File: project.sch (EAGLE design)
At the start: 43 parts, among them U1 DSPIC33FJ64MC804-H/PT, U2 TB6612FNG,C,8,EL, Y1 ABM8-20.000MHZ-B2-T

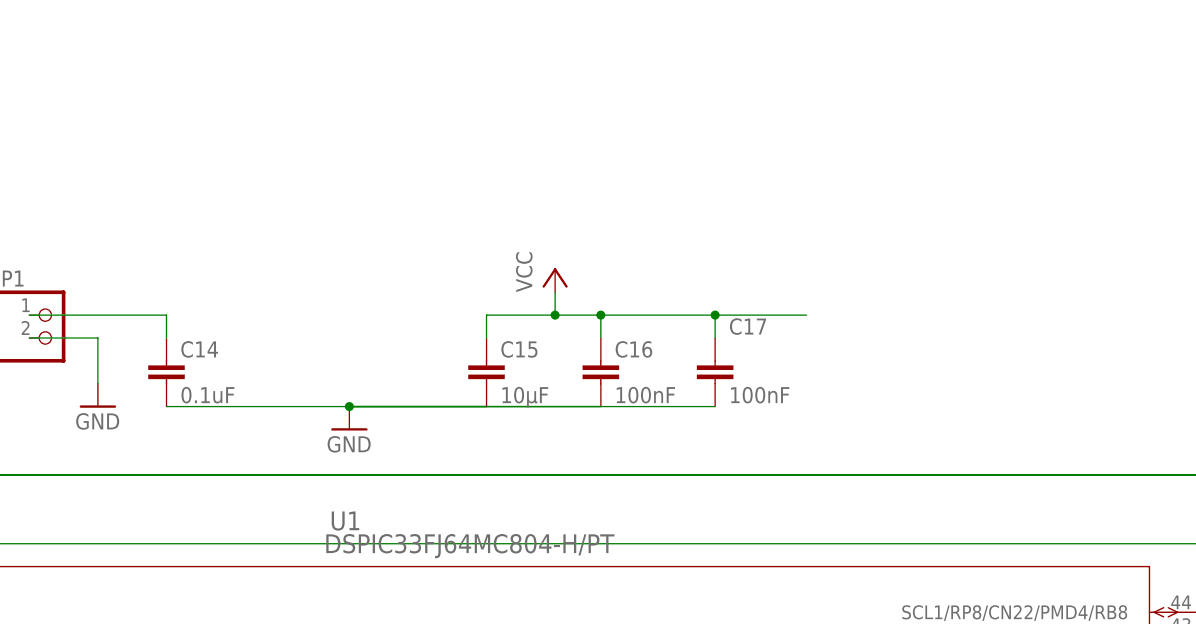
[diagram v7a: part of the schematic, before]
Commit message: Linear Regulator Added
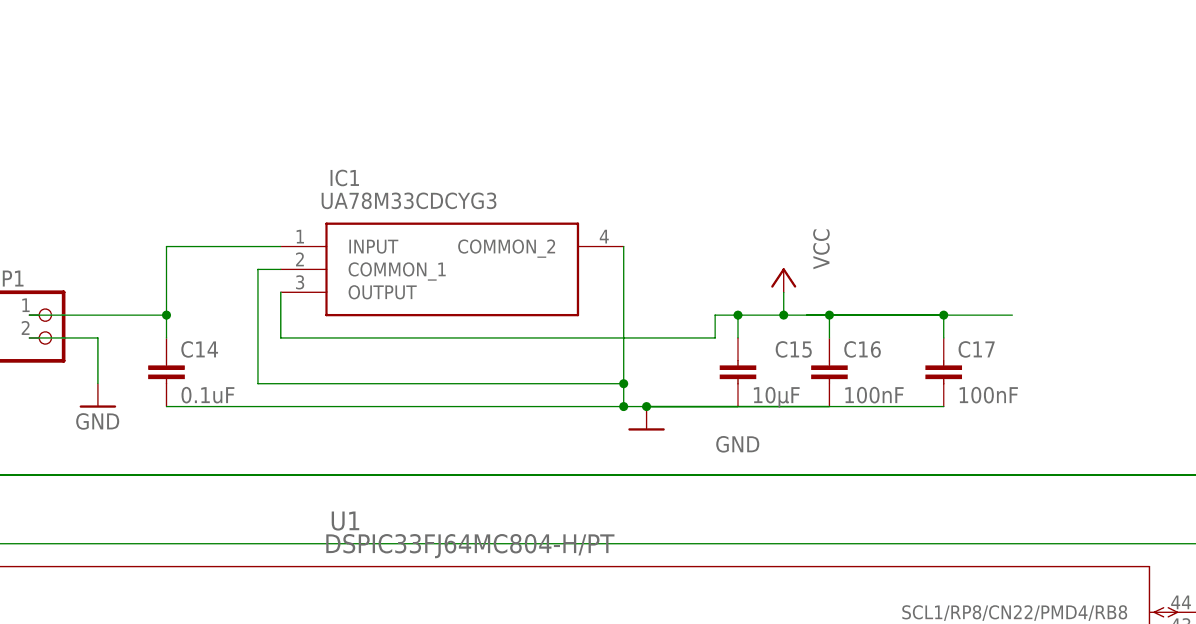
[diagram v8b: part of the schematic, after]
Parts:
- added IC1: UA78M33CDCYG3, UA78M33CDCYG3:UA78M33CDCYG3
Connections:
- net GND: now also IC1.COMMON_1, IC1.COMMON_2
- net N$6: now also IC1.INPUT
- net VCC: now also IC1.OUTPUT
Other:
- moved on the sheet: C15, C16, C17
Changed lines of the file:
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@@
 <part name="GND14" library="supply1" library_urn="urn:adsk.eagle:library:371" deviceset="GND" device=""/>
 <part name="GND15" library="supply1" library_urn="urn:adsk.eagle:library:371" deviceset="GND" device=""/>
+<part name="IC1" library="UA78M33CDCYG3" deviceset="UA78M33CDCYG3" device=""/>
 </parts>
 <sheets>
@@
 <attribute name="VALUE" x="9.144" y="48.641" size="1.778" layer="96"/>
 </instance>
-<instance part="C15" gate="G$1" x="43.18" y="53.34" smashed="yes">
-<attribute name="NAME" x="44.704" y="53.721" size="1.778" layer="95"/>
-<attribute name="VALUE" x="44.704" y="48.641" size="1.778" layer="96"/>
-</instance>
-<instance part="C16" gate="G$1" x="55.88" y="53.34" smashed="yes">
-<attribute name="NAME" x="57.404" y="53.721" size="1.778" layer="95"/>
-<attribute name="VALUE" x="57.404" y="48.641" size="1.778" layer="96"/>
-</instance>
-<instance part="C17" gate="G$1" x="68.58" y="53.34" smashed="yes">
-<attribute name="NAME" x="70.104" y="56.261" size="1.778" layer="95"/>
-<attribute name="VALUE" x="70.104" y="48.641" size="1.778" layer="96"/>
-</instance>
-<instance part="P+5" gate="VCC" x="50.8" y="63.5" smashed="yes">
-<attribute name="VALUE" x="48.26" y="60.96" size="1.778" layer="96" rot="R90"/>
-</instance>
-<instance part="GND19" gate="1" x="27.94" y="45.72" smashed="yes">
-<attribute name="VALUE" x="25.4" y="43.18" size="1.778" layer="96"/>
+<instance part="C15" gate="G$1" x="71.12" y="53.34" smashed="yes">
+<attribute name="NAME" x="75.184" y="53.721" size="1.778" layer="95"/>
+<attribute name="VALUE" x="72.644" y="48.641" size="1.778" layer="96"/>
+</instance>
+<instance part="C16" gate="G$1" x="81.28" y="53.34" smashed="yes">
+<attribute name="NAME" x="82.804" y="53.721" size="1.778" layer="95"/>
+<attribute name="VALUE" x="82.804" y="48.641" size="1.778" layer="96"/>
+</instance>
+<instance part="C17" gate="G$1" x="93.98" y="53.34" smashed="yes">
+<attribute name="NAME" x="95.504" y="53.721" size="1.778" layer="95"/>
+<attribute name="VALUE" x="95.504" y="48.641" size="1.778" layer="96"/>
+</instance>
+<instance part="P+5" gate="VCC" x="76.2" y="63.5" smashed="yes">
+<attribute name="VALUE" x="81.28" y="63.5" size="1.778" layer="96" rot="R90"/>
+</instance>
+<instance part="GND19" gate="1" x="60.96" y="45.72" smashed="yes">
+<attribute name="VALUE" x="68.58" y="43.18" size="1.778" layer="96"/>
 </instance>
 <instance part="GND20" gate="1" x="0" y="48.26" smashed="yes">
@@
 <instance part="GND15" gate="1" x="251.46" y="33.02" smashed="yes">
 <attribute name="VALUE" x="248.92" y="30.48" size="1.778" layer="96"/>
+</instance>
+<instance part="IC1" gate="G$1" x="20.32" y="66.04" smashed="yes">
+<attribute name="NAME" x="29.21" y="73.66" size="1.778" layer="95" rot="R180" align="center-left"/>
+<attribute name="VALUE" x="44.45" y="71.12" size="1.778" layer="96" rot="R180" align="center-left"/>
 </instance>
 </instances>
@@
 <segment>
 <pinref part="C15" gate="G$1" pin="1"/>
-<wire x1="43.18" y1="58.42" x2="50.8" y2="58.42" width="0.1524" layer="91"/>
-<wire x1="50.8" y1="58.42" x2="55.88" y2="58.42" width="0.1524" layer="91"/>
-<wire x1="55.88" y1="58.42" x2="68.58" y2="58.42" width="0.1524" layer="91"/>
-<wire x1="68.58" y1="58.42" x2="78.74" y2="58.42" width="0.1524" layer="91"/>
-<wire x1="43.18" y1="58.42" x2="43.18" y2="55.88" width="0.1524" layer="91"/>
+<wire x1="71.12" y1="58.42" x2="76.2" y2="58.42" width="0.1524" layer="91"/>
+<wire x1="76.2" y1="58.42" x2="81.28" y2="58.42" width="0.1524" layer="91"/>
+<wire x1="81.28" y1="58.42" x2="93.98" y2="58.42" width="0.1524" layer="91"/>
+<wire x1="93.98" y1="58.42" x2="78.74" y2="58.42" width="0.1524" layer="91"/>
+<wire x1="71.12" y1="58.42" x2="71.12" y2="55.88" width="0.1524" layer="91"/>
 <pinref part="C16" gate="G$1" pin="1"/>
-<wire x1="55.88" y1="58.42" x2="55.88" y2="55.88" width="0.1524" layer="91"/>
-<junction x="55.88" y="58.42"/>
+<wire x1="81.28" y1="58.42" x2="81.28" y2="55.88" width="0.1524" layer="91"/>
+<junction x="81.28" y="58.42"/>
 <pinref part="C17" gate="G$1" pin="1"/>
-<wire x1="68.58" y1="58.42" x2="68.58" y2="55.88" width="0.1524" layer="91"/>
-<junction x="68.58" y="58.42"/>
+<wire x1="93.98" y1="58.42" x2="93.98" y2="55.88" width="0.1524" layer="91"/>
+<junction x="93.98" y="58.42"/>
 <pinref part="P+5" gate="VCC" pin="VCC"/>
-<wire x1="50.8" y1="60.96" x2="50.8" y2="58.42" width="0.1524" layer="91"/>
-<junction x="50.8" y="58.42"/>
+<wire x1="76.2" y1="60.96" x2="76.2" y2="58.42" width="0.1524" layer="91"/>
+<junction x="76.2" y="58.42"/>
+<wire x1="93.98" y1="58.42" x2="101.6" y2="58.42" width="0.1524" layer="91"/>
+<pinref part="IC1" gate="G$1" pin="OUTPUT"/>
+<wire x1="20.32" y1="60.96" x2="20.32" y2="55.88" width="0.1524" layer="91"/>
+<wire x1="20.32" y1="55.88" x2="68.58" y2="55.88" width="0.1524" layer="91"/>
+<wire x1="68.58" y1="55.88" x2="68.58" y2="58.42" width="0.1524" layer="91"/>
+<wire x1="68.58" y1="58.42" x2="71.12" y2="58.42" width="0.1524" layer="91"/>
+<junction x="71.12" y="58.42"/>
 </segment>
 <segment>
@@
 <segment>
 <pinref part="GND19" gate="1" pin="GND"/>
+<junction x="60.96" y="48.26"/>
+<pinref part="C15" gate="G$1" pin="2"/>
+<wire x1="71.12" y1="48.26" x2="60.96" y2="48.26" width="0.1524" layer="91"/>
+<pinref part="C16" gate="G$1" pin="2"/>
+<wire x1="81.28" y1="48.26" x2="60.96" y2="48.26" width="0.1524" layer="91"/>
+<pinref part="C17" gate="G$1" pin="2"/>
+<wire x1="93.98" y1="48.26" x2="60.96" y2="48.26" width="0.1524" layer="91"/>
 <pinref part="C14" gate="G$1" pin="2"/>
-<wire x1="7.62" y1="48.26" x2="27.94" y2="48.26" width="0.1524" layer="91"/>
-<junction x="27.94" y="48.26"/>
-<pinref part="C15" gate="G$1" pin="2"/>
-<wire x1="43.18" y1="48.26" x2="27.94" y2="48.26" width="0.1524" layer="91"/>
-<pinref part="C16" gate="G$1" pin="2"/>
-<wire x1="55.88" y1="48.26" x2="27.94" y2="48.26" width="0.1524" layer="91"/>
-<pinref part="C17" gate="G$1" pin="2"/>
-<wire x1="68.58" y1="48.26" x2="27.94" y2="48.26" width="0.1524" layer="91"/>
+<wire x1="58.42" y1="48.26" x2="60.96" y2="48.26" width="0.1524" layer="91"/>
+<wire x1="7.62" y1="48.26" x2="58.42" y2="48.26" width="0.1524" layer="91"/>
+<pinref part="IC1" gate="G$1" pin="COMMON_1"/>
+<wire x1="20.32" y1="63.5" x2="17.78" y2="63.5" width="0.1524" layer="91"/>
+<wire x1="17.78" y1="63.5" x2="17.78" y2="50.8" width="0.1524" layer="91"/>
+<wire x1="17.78" y1="50.8" x2="58.42" y2="50.8" width="0.1524" layer="91"/>
+<wire x1="58.42" y1="50.8" x2="58.42" y2="48.26" width="0.1524" layer="91"/>
+<junction x="58.42" y="48.26"/>
+<pinref part="IC1" gate="G$1" pin="COMMON_2"/>
+<wire x1="58.42" y1="66.04" x2="58.42" y2="50.8" width="0.1524" layer="91"/>
+<junction x="58.42" y="50.8"/>
 </segment>
 <segment>
@@
 <pinref part="C14" gate="G$1" pin="1"/>
 <wire x1="7.62" y1="58.42" x2="7.62" y2="55.88" width="0.1524" layer="91"/>
-</segment>
-</net>
+<pinref part="IC1" gate="G$1" pin="INPUT"/>
+<wire x1="20.32" y1="66.04" x2="7.62" y2="66.04" width="0.1524" layer="91"/>
+<wire x1="7.62" y1="66.04" x2="7.62" y2="58.42" width="0.1524" layer="91"/>
+<junction x="7.62" y="58.42"/>
+</segment>
+</net>
